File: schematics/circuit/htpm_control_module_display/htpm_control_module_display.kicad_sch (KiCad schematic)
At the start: 58 parts, among them J1 Conn_01x10_Socket, J2 Conn_01x10_Socket

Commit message: Updated comments on the HTPm CONTROL Module Display.
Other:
- title: HTP!m CONTROL Display -> HTP!m CONTROL Module Display

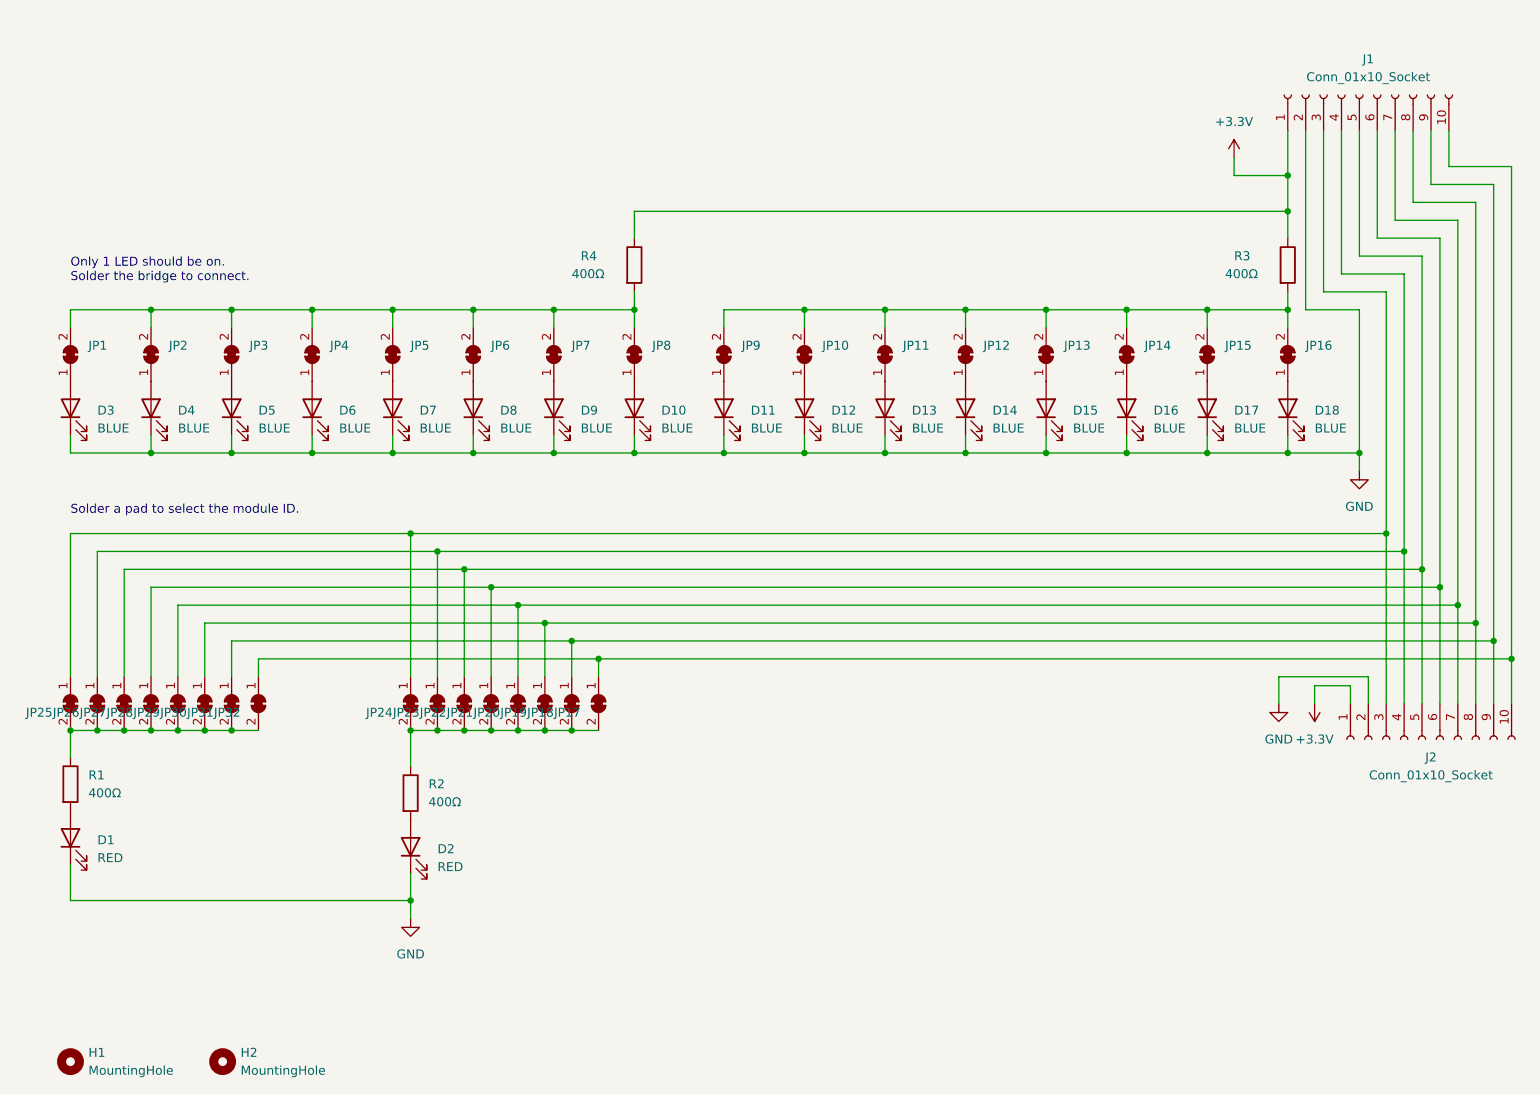
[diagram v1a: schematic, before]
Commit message: Updated recommended R and V values.
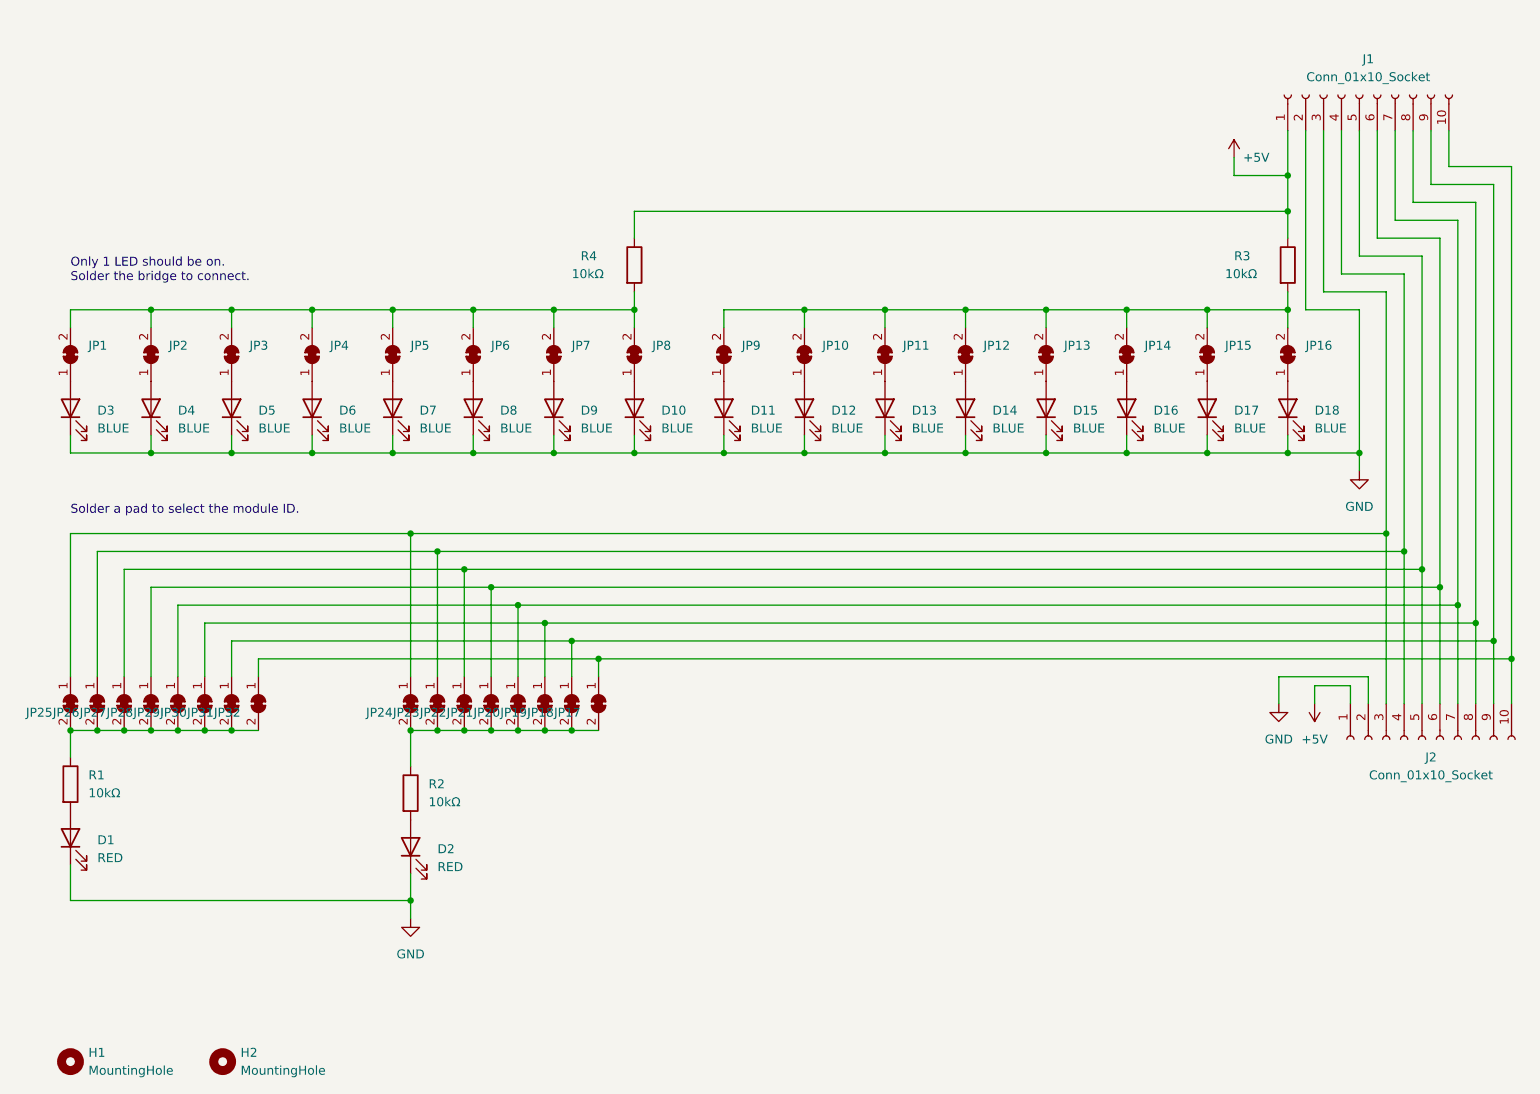
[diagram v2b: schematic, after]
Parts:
- R1, R2, R3, R4: value 400Ω -> 10kΩ
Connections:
- net +3.3V: no longer J2.1 (Pin_1)
- new net +5V: J2.1 (Pin_1)
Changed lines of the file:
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@@
       (effects (font (size 1.27 1.27)) (justify left))
     )
-    (property "Value" "400Ω" (at 58.42 125.73 0)
+    (property "Value" "10kΩ" (at 58.42 125.73 0)
       (effects (font (size 1.27 1.27)) (justify left))
     )
@@
       (effects (font (size 1.27 1.27)) (justify left))
     )
-    (property "Value" "400Ω" (at 106.68 127 0)
+    (property "Value" "10kΩ" (at 106.68 127 0)
       (effects (font (size 1.27 1.27)) (justify left))
     )
@@
     )
   )
-  (symbol (lib_id "power:+3.3V") (at 232.41 113.03 180) (unit 1)
-    (in_bom yes) (on_board yes) (dnp no) (fields_autoplaced)
-    (property "Reference" "#PWR04" (at 232.41 109.22 0)
-      (effects (font (size 1.27 1.27)) hide)
-    )
-    (property "Value" "+3.3V" (at 232.41 118.11 0)
+  (symbol (lib_id "power:+5V") (at 232.41 113.03 180) (unit 1)
+    (in_bom yes) (on_board yes) (dnp no) (fields_autoplaced)
+    (property "Reference" "#PWR0101" (at 232.41 109.22 0)
+      (effects (font (size 1.27 1.27)) hide)
+    )
+    (property "Value" "+5V" (at 232.41 118.11 0)
       (effects (font (size 1.27 1.27)))
     )
@@
       (project "htpm_control_module_display"
         (path "/5d804e4b-c61d-47d3-9254-644534119e0a"
-          (reference "#PWR04") (unit 1)
+          (reference "#PWR0101") (unit 1)
         )
       )
@@
       (effects (font (size 1.27 1.27)) (justify left))
     )
-    (property "Value" "400Ω" (at 127 52.07 0)
+    (property "Value" "10kΩ" (at 127 52.07 0)
       (effects (font (size 1.27 1.27)) (justify left))
     )
@@
       (effects (font (size 1.27 1.27)) (justify left))
     )
-    (property "Value" "400Ω" (at 219.71 52.07 0)
+    (property "Value" "10kΩ" (at 219.71 52.07 0)
       (effects (font (size 1.27 1.27)) (justify left))
     )
@@
   (symbol (lib_id "power:+3.3V") (at 220.98 35.56 0) (unit 1)
     (in_bom yes) (on_board yes) (dnp no)
-    (property "Reference" "#PWR02" (at 220.98 39.37 0)
-      (effects (font (size 1.27 1.27)) hide)
-    )
-    (property "Value" "+3.3V" (at 220.98 30.48 0)
-      (effects (font (size 1.27 1.27)))
+    (property "Reference" "#PWR06" (at 220.98 39.37 0)
+      (effects (font (size 1.27 1.27)) hide)
+    )
+    (property "Value" "+5V" (at 222.25 35.56 0)
+      (effects (font (size 1.27 1.27)) (justify left))
     )
     (property "Footprint" "" (at 220.98 35.56 0)
@@
       (project "htpm_control_module_display"
         (path "/5d804e4b-c61d-47d3-9254-644534119e0a"
-          (reference "#PWR02") (unit 1)
-        )
-      )
+          (reference "#PWR06") (unit 1)
+        )
+      )

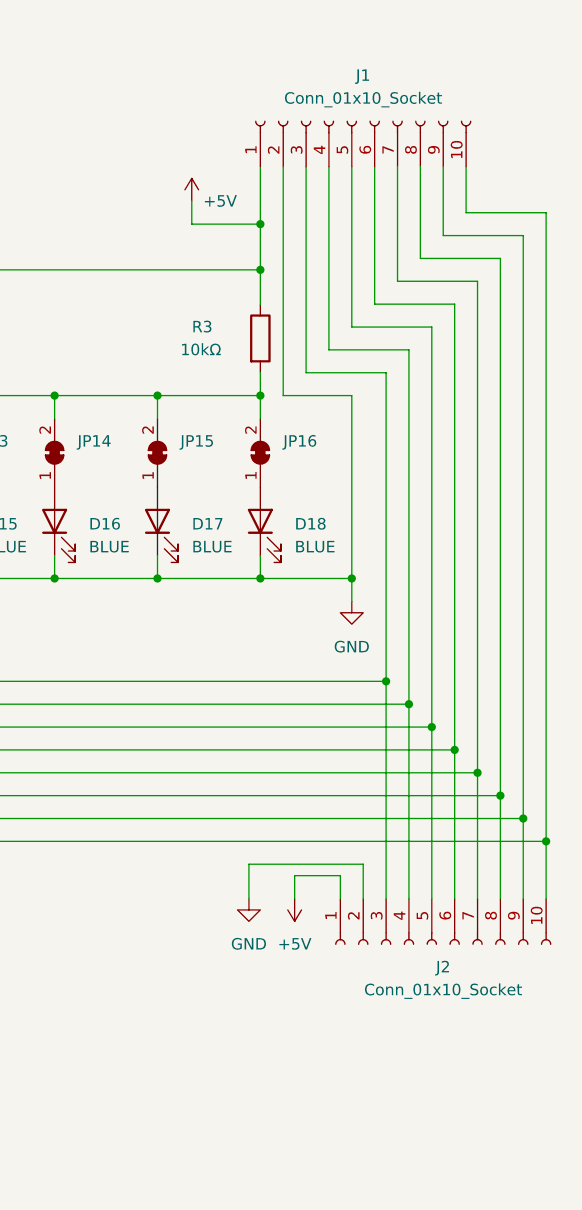
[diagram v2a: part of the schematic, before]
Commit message: Updated circuit annotations.
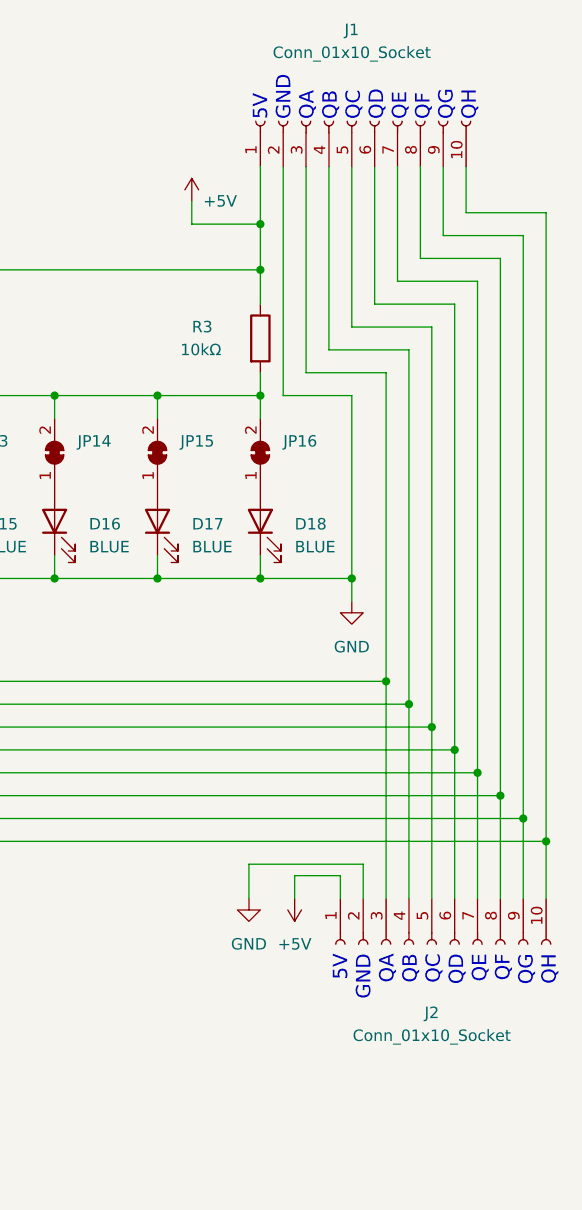
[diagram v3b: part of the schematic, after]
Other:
- note added: "5V GND QA QB QC QD QE QF QG QH"
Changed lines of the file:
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@@
     (effects (font (size 1.27 1.27)) (justify left bottom))
+  )
+  (text "5V\nGND\nQA\nQB\nQC\nQD\nQE\nQF\nQG\nQH" (at 261.62 119.38 90)
+    (effects (font (size 1.6 1.6)) (justify right bottom))
+  )
+  (text "5V\nGND\nQA\nQB\nQC\nQD\nQE\nQF\nQG\nQH" (at 252.73 26.67 90)
+    (effects (font (size 1.6 1.6)) (justify left bottom))
   )
   (text "Only 1 LED should be on.\nSolder the bridge to connect."
@@
   )
   (symbol (lib_id "Connector:Conn_01x10_Socket") (at 238.76 26.67 90) (unit 1)
-    (in_bom yes) (on_board yes) (dnp no) (fields_autoplaced)
-    (property "Reference" "J1" (at 240.03 21.59 90)
+    (in_bom yes) (on_board yes) (dnp no)
+    (property "Reference" "J1" (at 238.76 16.51 90)
       (effects (font (size 1.27 1.27)))
     )
-    (property "Value" "Conn_01x10_Socket" (at 240.03 24.13 90)
+    (property "Value" "Conn_01x10_Socket" (at 238.76 19.05 90)
       (effects (font (size 1.27 1.27)))
     )
@@
   (symbol (lib_id "Connector:Conn_01x10_Socket") (at 247.65 118.11 90) (mirror x) (unit 1)
     (in_bom yes) (on_board yes) (dnp no)
-    (property "Reference" "J2" (at 248.92 120.65 90)
+    (property "Reference" "J2" (at 247.65 125.73 90)
       (effects (font (size 1.27 1.27)))
     )
-    (property "Value" "Conn_01x10_Socket" (at 248.92 123.19 90)
+    (property "Value" "Conn_01x10_Socket" (at 247.65 128.27 90)
       (effects (font (size 1.27 1.27)))
     )
